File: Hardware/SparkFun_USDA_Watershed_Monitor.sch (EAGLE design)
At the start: 112 parts, among them J10 QWIIC_RIGHT_ANGLE, J3 QWIIC_RIGHT_ANGLE, J4 U.FL, J5 RJ45, J7 RJ45, J9 RJ45, Q1 20V/4.2A/52mΩ/1.4W, Q2 20V/0.2A/8MHz/1.2Ω/1Vth, Q3 20V/0.2A/8MHz/1.2Ω/1Vth, Q4 20V/0.2A/8MHz/1.2Ω/1Vth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

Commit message: Connect RFM95W pins
Somebody forgot to connect them...
Connect ESP32's IO5 and IO15 (both internally pulled high) to RFM's RESET and CS respectively
Connect ESP32's IO26 and IO27 to RFM's IO1 and IO0 respectively (IO2 not needed for LoRa)
ESP32's IO15, IO26, and IO27 are no longer broken out to RJ45 or headers
Add pullup resistor to ESP_EN
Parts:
- added R26: 100k, SparkFun-Resistors:100KOHM-0603-1/10W-1%
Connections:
- removed net ESP_IO15: J9.1, U1.CS2/IOA15
- removed net ESP_IO26: U1.DAC2/IOA26
- removed net ESP_IO27: U1.IOA27
- removed net ESP_IO5: U1.CS3/IO5
- removed net IO26: U11.!CS!
- removed net IO27: U11.DIO2
- removed net IO32: U11.DIO1
- removed net IO33: U11.DIO0
- new net !RFM_CS!: U1.CS2/IOA15, U11.!CS!
- new net RFM_IO0: U1.IOA27, U11.DIO0
- new net RFM_IO1: U1.DAC2/IOA26, U11.DIO1
- net !RFM_RST!: now also U1.CS3/IO5
- net 3.3V: now also R26.2
- net ESP_EN: now also R26.1
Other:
- moved on the sheet: BOOT, RESET
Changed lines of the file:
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@@
 <part name="GND59" library="SparkFun-PowerSymbols" deviceset="GND" device=""/>
 <part name="SUPPLY6" library="SparkFun-PowerSymbols" deviceset="3.3V" device=""/>
+<part name="R26" library="SparkFun-Resistors" deviceset="100KOHM" device="-0603-1/10W-1%" value="100k"/>
+<part name="SUPPLY47" library="SparkFun-PowerSymbols" deviceset="3.3V" device=""/>
 </parts>
 <sheets>
@@
 <attribute name="VALUE" x="264.16" y="7.366" size="1.778" layer="96" font="vector" align="top-center"/>
 </instance>
-<instance part="BOOT" gate="G$1" x="403.86" y="76.2" smashed="yes" rot="R180">
-<attribute name="NAME" x="403.86" y="74.676" size="1.778" layer="95" font="vector" rot="R180" align="bottom-center"/>
-</instance>
-<instance part="RESET" gate="G$1" x="365.76" y="76.2" smashed="yes" rot="R180">
-<attribute name="NAME" x="365.76" y="74.676" size="1.778" layer="95" font="vector" rot="R180" align="bottom-center"/>
-</instance>
-<instance part="GND53" gate="1" x="373.38" y="71.12" smashed="yes">
-<attribute name="VALUE" x="373.38" y="70.866" size="1.778" layer="96" font="vector" align="top-center"/>
-</instance>
-<instance part="GND54" gate="1" x="411.48" y="71.12" smashed="yes">
-<attribute name="VALUE" x="411.48" y="70.866" size="1.778" layer="96" font="vector" align="top-center"/>
+<instance part="BOOT" gate="G$1" x="403.86" y="71.12" smashed="yes" rot="R180">
+<attribute name="NAME" x="403.86" y="69.596" size="1.778" layer="95" font="vector" rot="R180" align="bottom-center"/>
+</instance>
+<instance part="RESET" gate="G$1" x="365.76" y="71.12" smashed="yes" rot="R180">
+<attribute name="NAME" x="365.76" y="69.596" size="1.778" layer="95" font="vector" rot="R180" align="bottom-center"/>
+</instance>
+<instance part="GND53" gate="1" x="373.38" y="66.04" smashed="yes">
+<attribute name="VALUE" x="373.38" y="65.786" size="1.778" layer="96" font="vector" align="top-center"/>
+</instance>
+<instance part="GND54" gate="1" x="411.48" y="66.04" smashed="yes">
+<attribute name="VALUE" x="411.48" y="65.786" size="1.778" layer="96" font="vector" align="top-center"/>
 </instance>
 <instance part="C24" gate="G$1" x="175.26" y="246.38" smashed="yes">
@@
 <instance part="SUPPLY6" gate="G$1" x="269.24" y="71.12" smashed="yes" rot="MR0">
 <attribute name="VALUE" x="269.24" y="73.914" size="1.778" layer="96" font="vector" rot="MR0" align="bottom-center"/>
+</instance>
+<instance part="R26" gate="G$1" x="358.14" y="78.74" smashed="yes" rot="R90">
+<attribute name="NAME" x="356.616" y="78.74" size="1.778" layer="95" font="vector" rot="R90" align="bottom-center"/>
+<attribute name="VALUE" x="359.664" y="78.74" size="1.778" layer="96" font="vector" rot="R90" align="top-center"/>
+</instance>
+<instance part="SUPPLY47" gate="G$1" x="358.14" y="86.36" smashed="yes">
+<attribute name="VALUE" x="358.14" y="89.154" size="1.778" layer="96" font="vector" align="bottom-center"/>
 </instance>
 </instances>
@@
 <pinref part="GND53" gate="1" pin="GND"/>
 <pinref part="RESET" gate="G$1" pin="1"/>
-<wire x1="370.84" y1="76.2" x2="373.38" y2="76.2" width="0.1524" layer="91" style="longdash"/>
-<wire x1="373.38" y1="76.2" x2="373.38" y2="73.66" width="0.1524" layer="91" style="longdash"/>
+<wire x1="370.84" y1="71.12" x2="373.38" y2="71.12" width="0.1524" layer="91" style="longdash"/>
+<wire x1="373.38" y1="71.12" x2="373.38" y2="68.58" width="0.1524" layer="91" style="longdash"/>
 </segment>
 <segment>
 <pinref part="GND54" gate="1" pin="GND"/>
 <pinref part="BOOT" gate="G$1" pin="1"/>
-<wire x1="408.94" y1="76.2" x2="411.48" y2="76.2" width="0.1524" layer="91" style="longdash"/>
-<wire x1="411.48" y1="76.2" x2="411.48" y2="73.66" width="0.1524" layer="91" style="longdash"/>
+<wire x1="408.94" y1="71.12" x2="411.48" y2="71.12" width="0.1524" layer="91" style="longdash"/>
+<wire x1="411.48" y1="71.12" x2="411.48" y2="68.58" width="0.1524" layer="91" style="longdash"/>
 </segment>
 <segment>
@@
 <pinref part="J8" gate="J1" pin="3"/>
 </segment>
+<segment>
+<pinref part="SUPPLY47" gate="G$1" pin="3.3V"/>
+<wire x1="358.14" y1="86.36" x2="358.14" y2="83.82" width="0.1524" layer="91"/>
+<pinref part="R26" gate="G$1" pin="2"/>
+</segment>
 </net>
 <net name="N$8" class="0">
@@
 <segment>
 <pinref part="RESET" gate="G$1" pin="2"/>
-<wire x1="360.68" y1="76.2" x2="358.14" y2="76.2" width="0.1524" layer="91"/>
-<label x="358.14" y="76.2" size="1.27" layer="95" font="vector" rot="R180" xref="yes"/>
+<wire x1="360.68" y1="71.12" x2="358.14" y2="71.12" width="0.1524" layer="91"/>
+<label x="355.6" y="71.12" size="1.27" layer="95" font="vector" rot="R180" xref="yes"/>
+<pinref part="R26" gate="G$1" pin="1"/>
+<wire x1="358.14" y1="71.12" x2="355.6" y2="71.12" width="0.1524" layer="91"/>
+<wire x1="358.14" y1="73.66" x2="358.14" y2="71.12" width="0.1524" layer="91"/>
+<junction x="358.14" y="71.12"/>
 </segment>
 </net>
@@
 </segment>
 </net>
-<net name="IO33" class="0">
+<net name="RFM_IO0" class="0">
 <segment>
 <pinref part="U11" gate="U1" pin="DIO0"/>
@@
 <label x="124.46" y="60.96" size="1.27" layer="95" font="vector" xref="yes"/>
 </segment>
-</net>
-<net name="IO32" class="0">
-<segment>
-<pinref part="U11" gate="U1" pin="DIO1"/>
-<wire x1="121.92" y1="58.42" x2="124.46" y2="58.42" width="0.1524" layer="91"/>
-<label x="124.46" y="58.42" size="1.27" layer="95" font="vector" xref="yes"/>
-</segment>
-</net>
-<net name="IO27" class="0">
-<segment>
-<pinref part="U11" gate="U1" pin="DIO2"/>
-<wire x1="121.92" y1="55.88" x2="124.46" y2="55.88" width="0.1524" layer="91"/>
-<label x="124.46" y="55.88" size="1.27" layer="95" font="vector" xref="yes"/>
+<segment>
+<pinref part="U1" gate="U1" pin="IOA27"/>
+<wire x1="53.34" y1="25.4" x2="55.88" y2="25.4" width="0.1524" layer="91"/>
+<label x="55.88" y="25.4" size="1.27" layer="95" font="vector" xref="yes"/>
 </segment>
 </net>
@@
 </segment>
 </net>
-<net name="IO26" class="0">
-<segment>
-<pinref part="U11" gate="U1" pin="!CS!"/>
-<wire x1="121.92" y1="33.02" x2="124.46" y2="33.02" width="0.1524" layer="91"/>
-<label x="124.46" y="33.02" size="1.27" layer="95" font="vector" xref="yes"/>
-</segment>
-</net>
 <net name="!RFM_RST!" class="0">
 <segment>
-<pinref part="U11" gate="U1" pin="!RESET"/>
 <wire x1="91.44" y1="58.42" x2="88.9" y2="58.42" width="0.1524" layer="91"/>
 <label x="88.9" y="58.42" size="1.27" layer="95" font="vector" rot="R180" xref="yes"/>
+<pinref part="U11" gate="U1" pin="!RESET"/>
+</segment>
+<segment>
+<pinref part="U1" gate="U1" pin="CS3/IO5"/>
+<wire x1="53.34" y1="66.04" x2="55.88" y2="66.04" width="0.1524" layer="91"/>
+<label x="55.88" y="66.04" size="1.27" layer="95" font="vector" xref="yes"/>
 </segment>
 </net>
@@
 <segment>
 <pinref part="BOOT" gate="G$1" pin="2"/>
-<wire x1="398.78" y1="76.2" x2="396.24" y2="76.2" width="0.1524" layer="91"/>
-<label x="396.24" y="76.2" size="1.27" layer="95" font="vector" rot="R180" xref="yes"/>
+<wire x1="398.78" y1="71.12" x2="396.24" y2="71.12" width="0.1524" layer="91"/>
+<label x="396.24" y="71.12" size="1.27" layer="95" font="vector" rot="R180" xref="yes"/>
 </segment>
 </net>
@@
 </segment>
 </net>
-<net name="ESP_IO5" class="0">
-<segment>
-<pinref part="U1" gate="U1" pin="CS3/IO5"/>
-<wire x1="53.34" y1="66.04" x2="55.88" y2="66.04" width="0.1524" layer="91"/>
-<label x="55.88" y="66.04" size="1.27" layer="95" font="vector" xref="yes"/>
-</segment>
-</net>
-<net name="ESP_IO15" class="0">
-<segment>
-<pinref part="U1" gate="U1" pin="CS2/IOA15"/>
-<wire x1="53.34" y1="60.96" x2="55.88" y2="60.96" width="0.1524" layer="91"/>
-<label x="55.88" y="60.96" size="1.27" layer="95" font="vector" xref="yes"/>
-</segment>
-<segment>
-<wire x1="304.8" y1="30.48" x2="299.72" y2="30.48" width="0.1524" layer="91"/>
-<label x="299.72" y="30.48" size="1.27" layer="95" font="vector" rot="R180" xref="yes"/>
-<pinref part="J9" gate="JP1" pin="1"/>
-</segment>
-</net>
 <net name="ESP_INT_COM" class="0">
 <segment>
@@
 </segment>
 </net>
-<net name="ESP_IO26" class="0">
+<net name="RFM_IO1" class="0">
 <segment>
 <pinref part="U1" gate="U1" pin="DAC2/IOA26"/>
@@
 <label x="55.88" y="27.94" size="1.27" layer="95" font="vector" xref="yes"/>
 </segment>
-</net>
-<net name="ESP_IO27" class="0">
-<segment>
-<pinref part="U1" gate="U1" pin="IOA27"/>
-<wire x1="53.34" y1="25.4" x2="55.88" y2="25.4" width="0.1524" layer="91"/>
-<label x="55.88" y="25.4" size="1.27" layer="95" font="vector" xref="yes"/>
+<segment>
+<pinref part="U11" gate="U1" pin="DIO1"/>
+<wire x1="121.92" y1="58.42" x2="124.46" y2="58.42" width="0.1524" layer="91"/>
+<label x="124.46" y="58.42" size="1.27" layer="95" font="vector" xref="yes"/>
 </segment>
 </net>
@@
 </segment>
 </net>
+<net name="!RFM_CS!" class="0">
+<segment>
+<pinref part="U1" gate="U1" pin="CS2/IOA15"/>
+<wire x1="53.34" y1="60.96" x2="55.88" y2="60.96" width="0.1524" layer="91"/>
+<label x="55.88" y="60.96" size="1.27" layer="95" font="vector" xref="yes"/>
+</segment>
+<segment>
+<wire x1="121.92" y1="33.02" x2="124.46" y2="33.02" width="0.1524" layer="91"/>
+<label x="124.46" y="33.02" size="1.27" layer="95" font="vector" xref="yes"/>
+<pinref part="U11" gate="U1" pin="!CS!"/>
+</segment>
+</net>

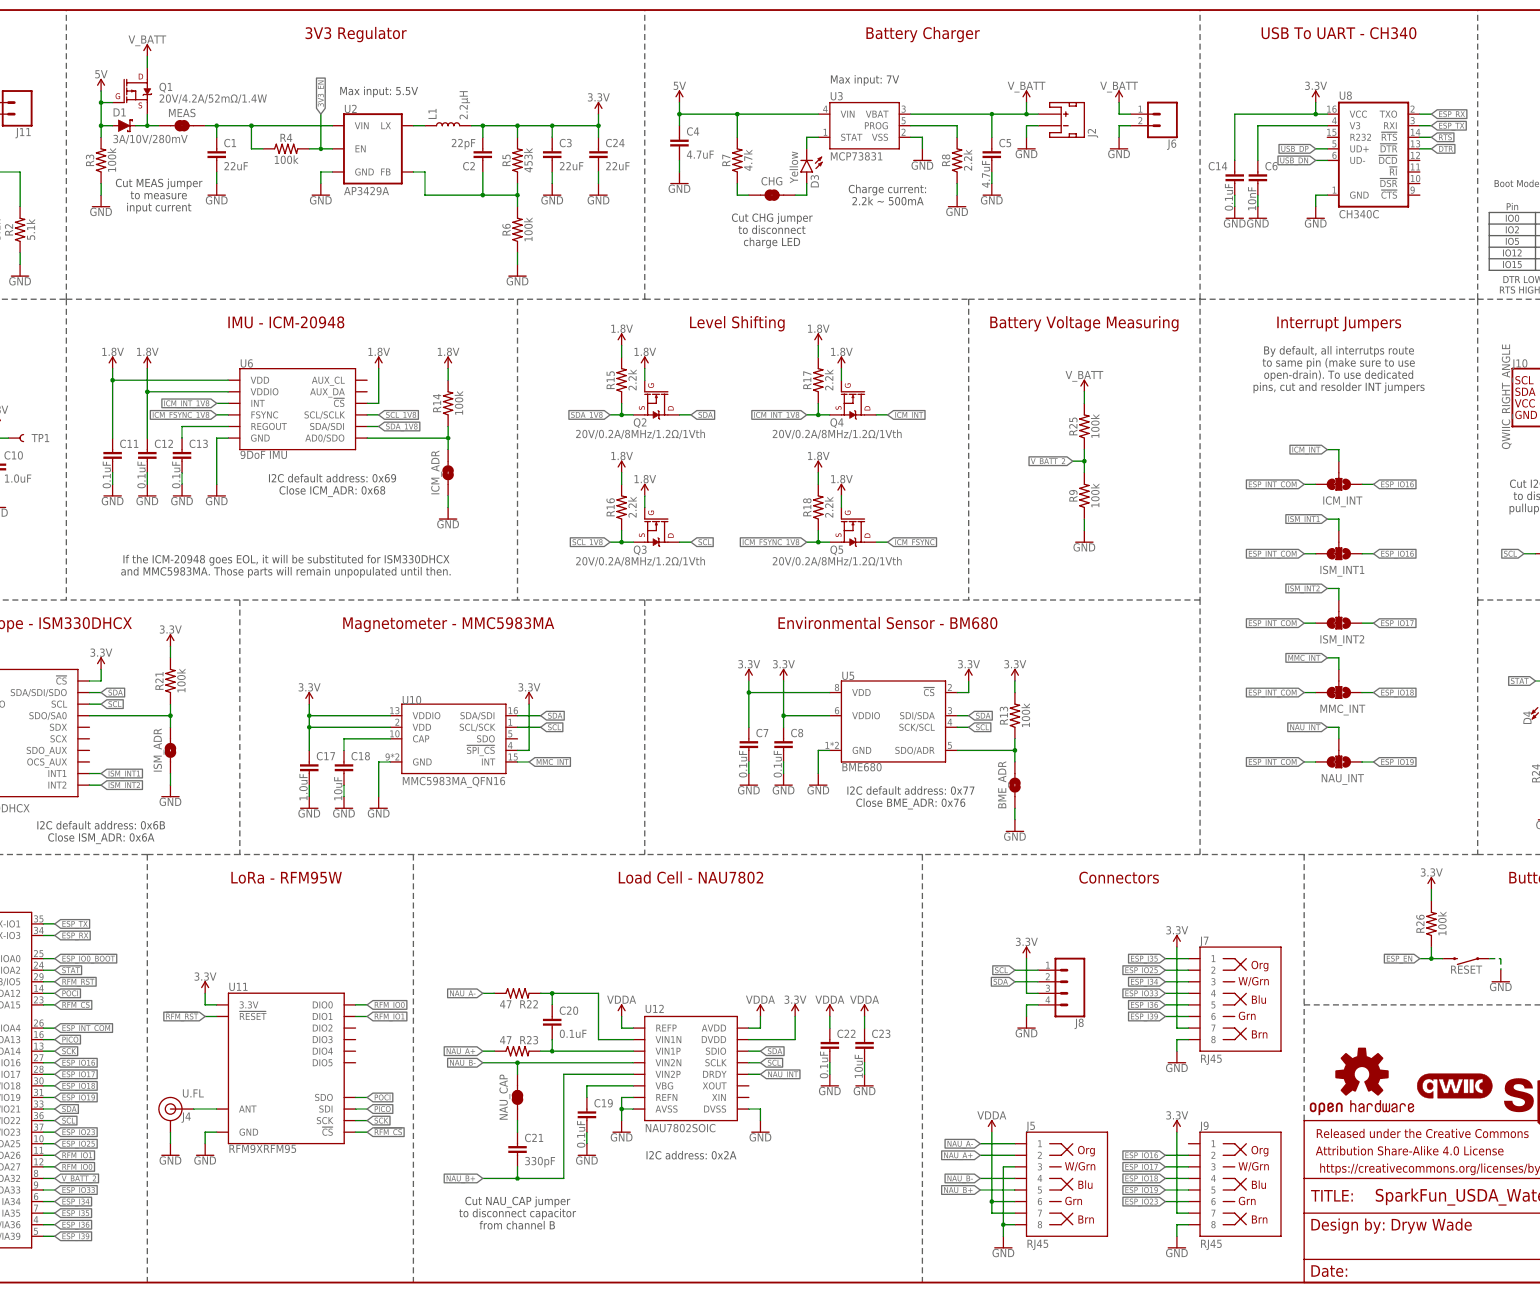
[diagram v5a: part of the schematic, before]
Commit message: Design review updates
Remove 3V3_EN and ICM's FSYNC nets (won't be used)
Add diode to NAU_INT (chip doesn't do open-drain)
Clarify interrupts needing to be open-drain, active high
Fix ICM interrupt level shifter output to be high-Z when input is low (or high-Z), and drive high when input is high
Add version number to copper
Add silk labels to RJ45s, and dashed lines connecting pinout to color code
Add IMU axis albels to silk
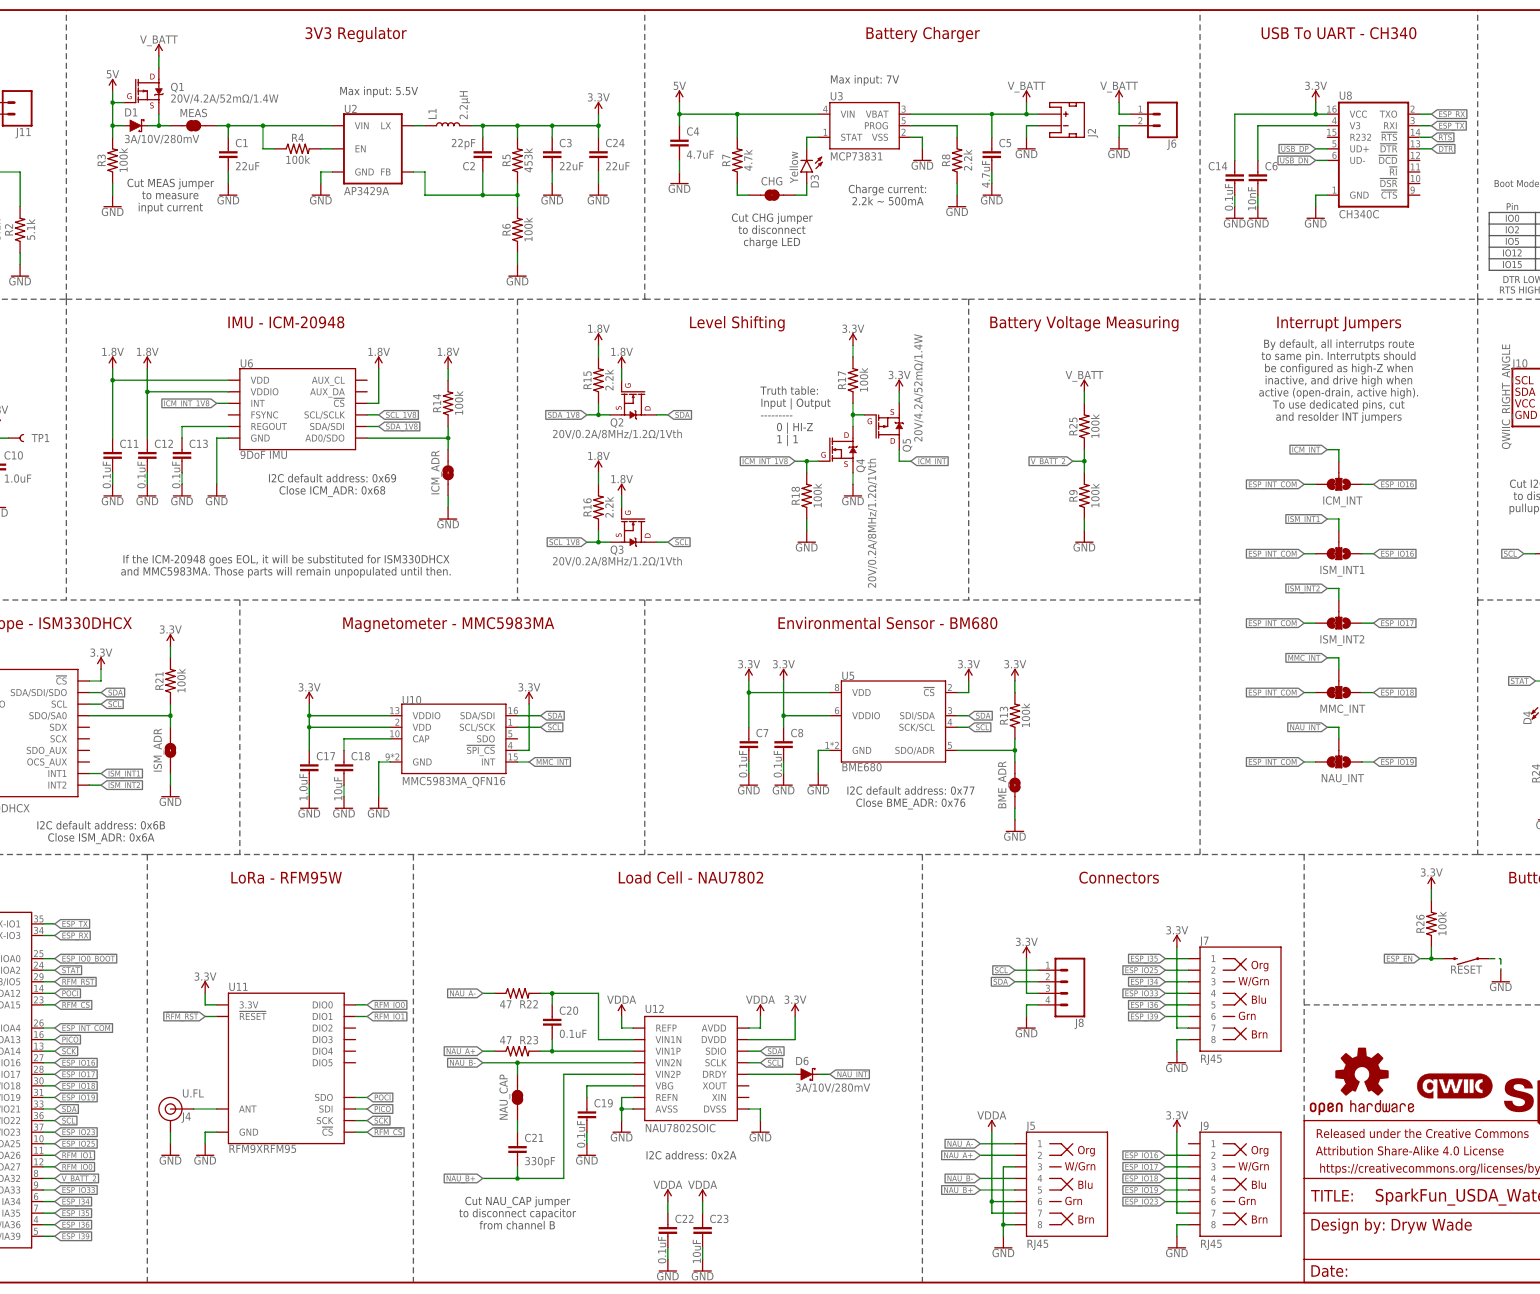
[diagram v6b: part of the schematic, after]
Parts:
- added D6: 3A/10V/280mV, SparkFun-DiscreteSemi:DIODE-SCHOTTKY-BAT60A
- Q5: value 20V/0.2A/8MHz/1.2Ω/1Vth -> 20V/4.2A/52mΩ/1.4W; device SparkFun-DiscreteSemi:MOSFET-NCH-RE1C002UNTCL -> SparkFun-DiscreteSemi:MOSFET_PCH-DMG2305UX-7
- R17, R18: value 2.2k -> 100k; device SparkFun-Resistors:2.2KOHM-0603-1/10W-1% -> SparkFun-Resistors:100KOHM-0603-1/10W-1%
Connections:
- removed net ICM_FSYNC: Q5.D
- removed net ICM_FSYNC_1V8: Q5.S, R18.1, U6.FSYNC
- new net N$29: D6.A, U12.DRDY
- new net N$30: Q4.D, Q5.G, R17.1
- net 1.8V: no longer Q4.G, Q5.G, R17.2, R18.2
- net 3.3V: now also Q5.S, R17.2
- net GND: now also Q4.S, R18.1
- net ICM_INT: now also Q5.D; no longer Q4.D
- net ICM_INT_1V8: now also Q4.G, R18.2; no longer Q4.S, R17.1
- net NAU_INT: now also D6.C; no longer U12.DRDY
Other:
- note added: "By default, all interrutps route to same pin. Interrutpts should be configured as high-Z when inactive, and drive high when active (open-drain, active high). To use dedicated pins, cut and resolder INT jumpers"
- note added: "Truth table: Input | Output --------- 0 | HI-Z 1 | 1"
- note removed: "By default, all interrutps route to same pin (make sure to use open-drain). To use dedicated pins, cut and resolder INT jumpers"
- moved on the sheet: C1, C22, C23, D1, MEAS, Q1, Q2, Q3, Q4, R15, R16, R17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

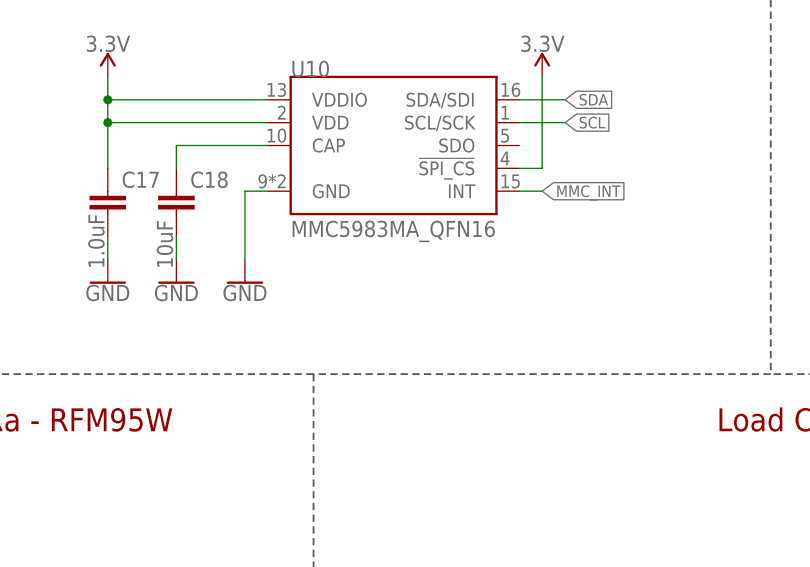
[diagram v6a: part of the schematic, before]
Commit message: Add MMC I2C address to schematic
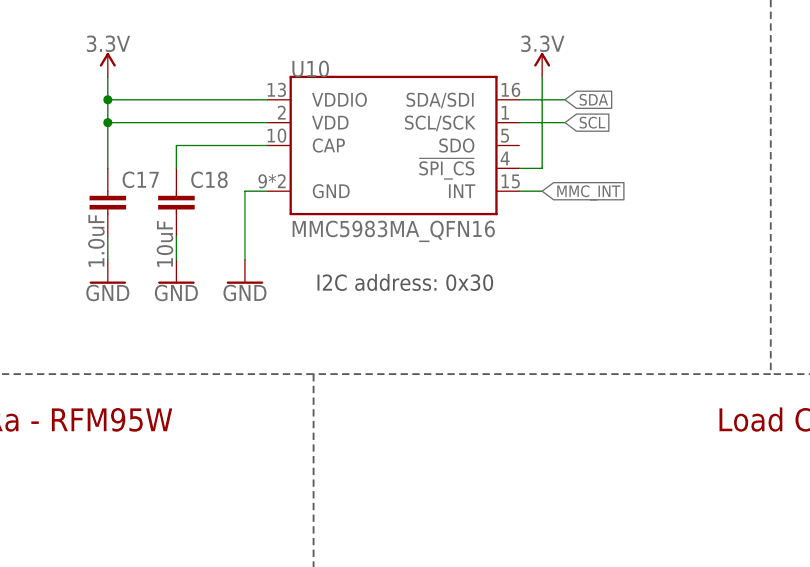
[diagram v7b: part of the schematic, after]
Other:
- note added: "I2C address: 0x30"
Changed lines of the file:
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@@
      0 | HI-Z
      1 | 1</text>
+<text x="144.78" y="104.14" size="1.778" layer="97" font="vector" align="center">I2C address: 0x30</text>
 </plain>
 <instances>
